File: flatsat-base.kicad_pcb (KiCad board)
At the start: 2 copper layers, 228.6 x 134.6 mm, 24 parts, among them J1 FFC2B28-24-G, J10 Conn_01x24_Male, J11 Conn_01x10_Male, J12 FFC2B28-10-G, J13 FFC2B28-10-G, J2 FFC2B28-10-G, J3 FFC2B28-10-G, J4 FFC2B28-10-G, J5 FFC2B28-10-G, J6 FFC2B28-10-G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

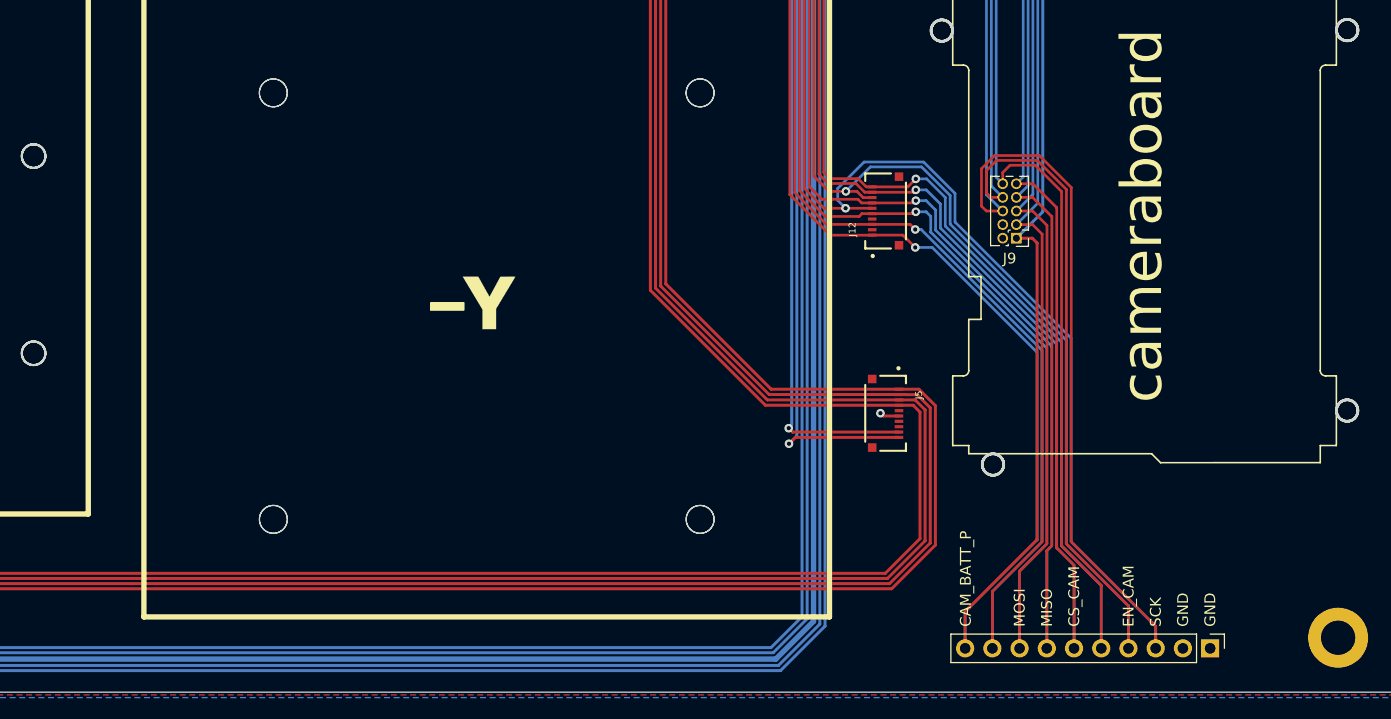
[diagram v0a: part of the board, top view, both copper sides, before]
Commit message: add battery connector and aligator clip points
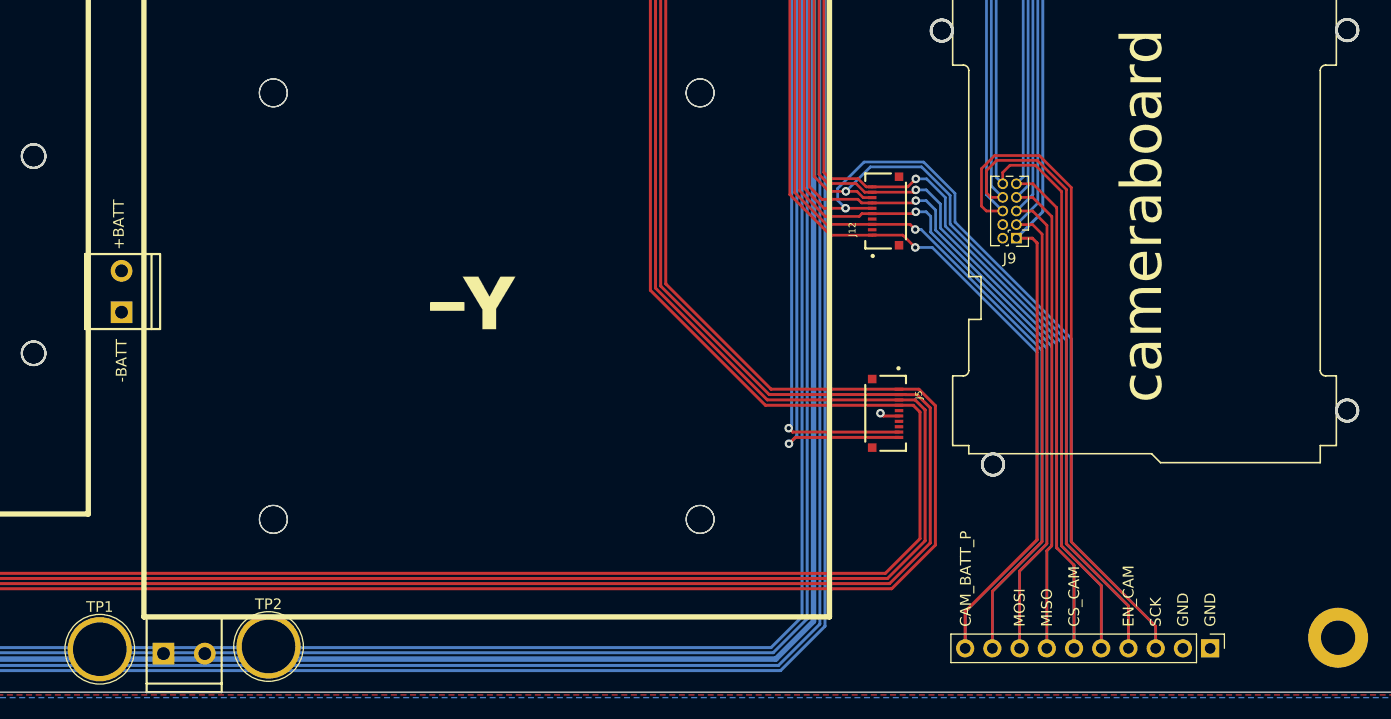
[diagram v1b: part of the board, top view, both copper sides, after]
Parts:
- added J14: Screw_Terminal_01x02, solarpanels:SCREWTERMINAL-3.5MM-2_LOCK, F.Cu at (138.7, 122.5)
- added J15: Screw_Terminal_01x02, solarpanels:SCREWTERMINAL-3.5MM-2_LOCK, F.Cu at (142.8, 154.6)
- added TP1: TestPoint, TestPoint:TestPoint_Plated_Hole_D5.0mm, F.Cu at (136.7, 154.2)
- added TP2: TestPoint, TestPoint:TestPoint_Plated_Hole_D5.0mm, F.Cu at (152.4, 153.9)
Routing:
- net COIL4_P: track 199.3 -> 740.9 mm, vias 1 -> 4
- net COIL6_N: track 314.1 -> 0.00 mm, vias 1 -> 0
- net BURN1: track 227.4 -> 0.00 mm, vias 2 -> 0
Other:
- board text added: "+BATT"
- board text added: "-BATT"

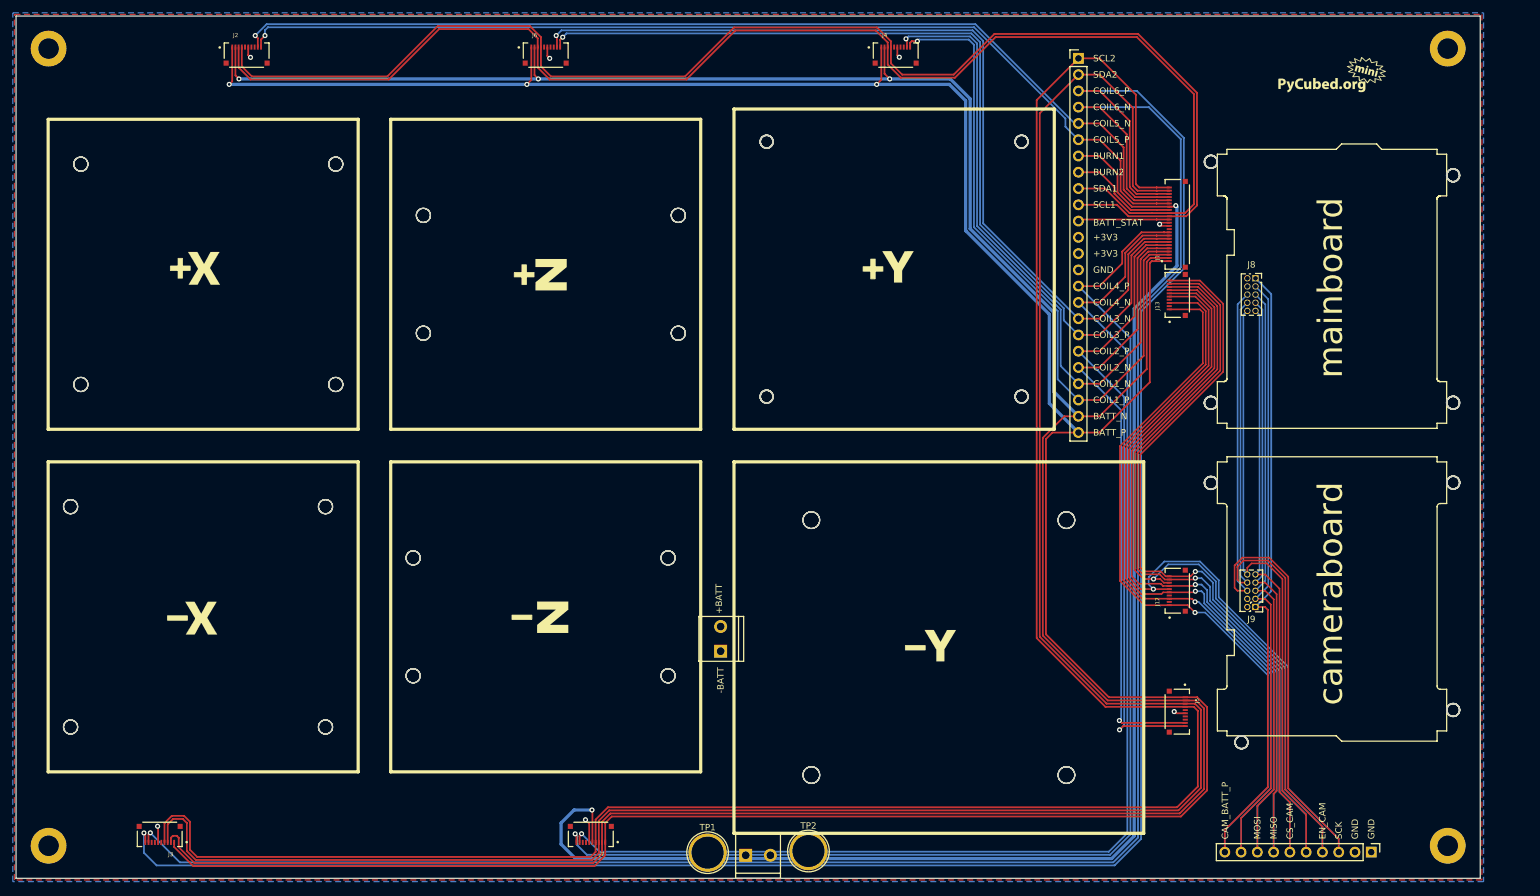
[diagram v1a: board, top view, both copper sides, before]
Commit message: Attachment points for BATT_P/BATT_N and routed
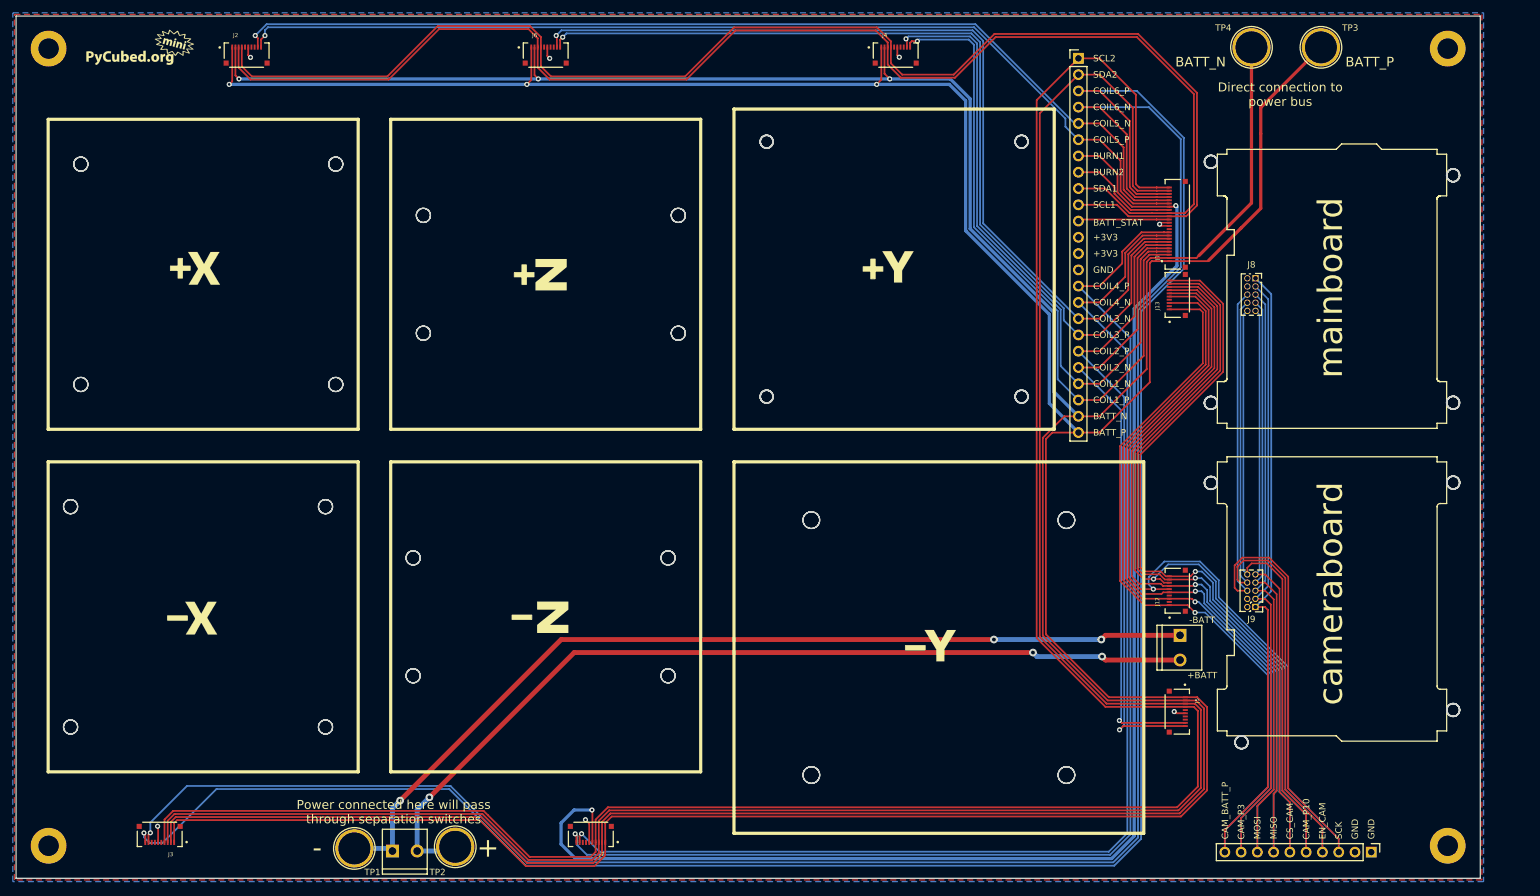
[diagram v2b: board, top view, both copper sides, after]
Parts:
- added TP3: TestPoint, TestPoint:TestPoint_Plated_Hole_D5.0mm, F.Cu at (232.4, 28.4)
- added TP4: TestPoint, TestPoint:TestPoint_Plated_Hole_D5.0mm, F.Cu at (221.6, 28.4)
- moved Ref** 186.2 mm to (54.9, 27.9)
- moved J14 71.8 mm to (210.4, 120.4), turned to -90 degrees
- moved J15 55.1 mm to (87.6, 153.9)
- moved TP2 55.1 mm to (97.3, 153.3)
- moved TP1 55.1 mm to (81.5, 153.5)
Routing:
- net COIL4_P: track 740.9 -> 199.3 mm, vias 4 -> 1
- net COIL6_N: track 0.00 -> 321.1 mm, vias 0 -> 1
- net BURN1: track 0.00 -> 227.4 mm, vias 0 -> 2
- net BATT_NOSWITCH_N: track 0.00 -> 146.9 mm, vias 0 -> 3
- net BATT_NOSWITCH_P: track 0.00 -> 142.4 mm, vias 0 -> 3
- net BATT_P: track 479.5 -> 530.4 mm
- net BATT_N: track 474.7 -> 518.5 mm
- net COIL6_P: track 321.5 -> 327.1 mm
- net SDA2: track 338.5 -> 336.9 mm
- net SCL2: track 343.1 -> 341.5 mm
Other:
- board text added: "+"
- board text added: "-"
- board text added: "CAM_P10"
- board text added: "CAM_P3"
- board text added: "Direct connection to power bus"
- board text added: "Power connected here will pass through separation switches"

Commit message: misc changes
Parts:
- moved H3 6.82 mm to (259.0, 153.3)
- moved H4 6.82 mm to (259.0, 28.9)
- moved J1 6.82 mm to (216.8, 56.3)
- moved J12 6.82 mm to (216.8, 113.5)
- moved J13 6.82 mm to (216.8, 67.3)
- moved J4 6.82 mm to (172.8, 29.9)
- moved J5 6.82 mm to (216.8, 132.4)
- moved J9 6.82 mm to (229.0, 116.1)
- moved Ref** 6.82 mm to (190.2, 63.9)
- moved TP3 6.82 mm to (239.2, 28.7)
- moved Ref** 6.82 mm to (61.7, 28.2)
- moved H1 6.82 mm to (40.6, 28.9)
- moved H2 6.82 mm to (40.6, 153.3)
- moved J15 6.82 mm to (94.4, 154.2)
- moved J2 6.82 mm to (71.5, 29.9)
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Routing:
- net COIL6_N: track 321.1 -> 297.7 mm
- net COIL6_P: track 327.1 -> 304.9 mm
- net BATT_NOSWITCH_N: track 146.9 -> 158.0 mm, vias 3 -> 0
- net COIL4_P: track 199.3 -> 191.3 mm
- net COIL4_N: track 195.8 -> 189.0 mm
- net BATT_N: track 518.5 -> 521.7 mm
- net SCL1: track 214.2 -> 211.1 mm
- net SDA1: track 214.2 -> 211.2 mm
- net BATT_P: track 530.4 -> 532.6 mm
- net +3V3: track 16.8 -> 15.1 mm
- net BURN1: track 227.4 -> 226.1 mm, vias 2 -> 1
- net BATT_NOSWITCH_P: track 142.4 -> 141.6 mm, vias 3 -> 0
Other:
- outline, holes or cut-outs redrawn
